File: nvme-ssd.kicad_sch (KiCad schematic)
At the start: 20 parts, among them J3 1-2199230-6

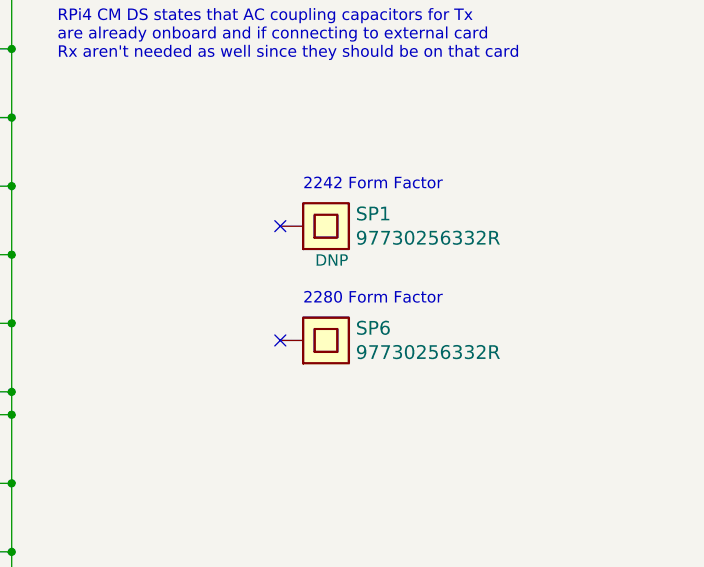
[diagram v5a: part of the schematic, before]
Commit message: Update SP1, SP6 symbol and footprint
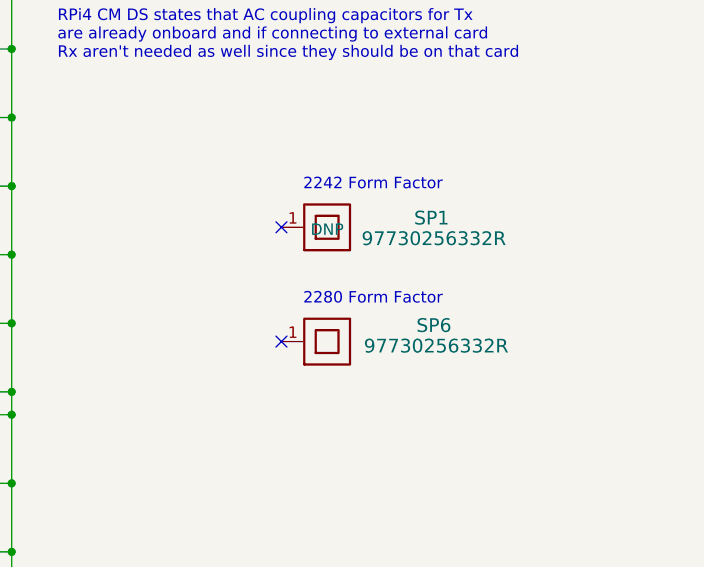
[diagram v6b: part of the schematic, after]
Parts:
- SP1, SP6: footprint scalenode-cm4-baseboard-footprints:97730256332R -> antmicro-footprints:97730256332R; symbol scalenode-cm4-baseboard:97730256332R -> antmicroMechanicalParts:97730256332R; Author (none) -> Antmicro; License (none) -> Apache-2.0; Manufacturer Wurth Elektronik -> Würth Elektronik
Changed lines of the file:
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@@
   (no_connect (at 133.35 85.09))
   (no_connect (at 133.35 52.07))
-  (no_connect (at 211.455 125.095))
+  (no_connect (at 211.582 125.222))
   (no_connect (at 171.45 120.65))
-  (no_connect (at 211.455 112.395))
+  (no_connect (at 211.582 112.522))
   (no_connect (at 171.45 102.87))
   (no_connect (at 171.45 95.25))
@@
     (pin "2")
   )
-  (symbol (lib_id "scalenode-cm4-baseboard:97730256332R") (at 216.535 112.395 0) (unit 1)
+  (symbol (lib_id "antmicroMechanicalParts:97730256332R") (at 211.582 112.522 0) (unit 1)
     (in_bom yes) (on_board yes)
-    (property "Reference" "SP1" (id 0) (at 219.837 111.0488 0)
+    (property "Reference" "SP1" (id 0) (at 226.314 111.506 0)
       (effects (font (size 1.524 1.524)) (justify left))
     )
-    (property "Value" "97730256332R" (id 1) (at 219.837 113.7412 0)
+    (property "Value" "97730256332R" (id 1) (at 220.472 113.792 0)
       (effects (font (size 1.524 1.524)) (justify left))
     )
-    (property "Footprint" "scalenode-cm4-baseboard-footprints:97730256332R" (id 2) (at 220.345 106.045 0)
-      (effects (font (size 1.524 1.524)) hide)
+    (property "Footprint" "antmicro-footprints:97730256332R" (id 2) (at 234.442 120.142 0)
+      (effects (font (size 1.27 1.27) (thickness 0.15)) (justify left bottom) hide)
     )
-    (property "Datasheet" "" (id 3) (at 216.535 112.395 0)
-      (effects (font (size 1.524 1.524)) hide)
+    (property "Datasheet" "" (id 3) (at 234.442 122.682 0)
+      (effects (font (size 1.27 1.27) (thickness 0.15)) (justify left bottom) hide)
     )
-    (property "Manufacturer" "Wurth Elektronik" (id 4) (at 216.535 112.395 0)
-      (effects (font (size 1.27 1.27)) hide)
+    (property "Manufacturer" "Würth Elektronik" (id 4) (at 234.442 125.222 0)
+      (effects (font (size 1.27 1.27) (thickness 0.15)) (justify left bottom) hide)
     )
-    (property "MPN" "97730256332R" (id 5) (at 216.535 112.395 0)
-      (effects (font (size 1.27 1.27)) hide)
+    (property "MPN" "97730256332R" (id 5) (at 234.442 127.762 0)
+      (effects (font (size 1.27 1.27) (thickness 0.15)) (justify left bottom) hide)
+    )
+    (property "DNP" "DNP" (id 6) (at 216.662 112.776 0))
+    (property "Author" "Antmicro" (id 7) (at 234.442 130.302 0)
+      (effects (font (size 1.27 1.27) (thickness 0.15)) (justify left bottom) hide)
+    )
+    (property "License" "Apache-2.0" (id 8) (at 234.442 132.842 0)
+      (effects (font (size 1.27 1.27) (thickness 0.15)) (justify left bottom) hide)
     )
-    (property "DNP" "DNP" (id 6) (at 217.17 116.205 0))
     (pin "1")
   )
-  (symbol (lib_id "scalenode-cm4-baseboard:97730256332R") (at 216.535 125.095 0) (unit 1)
+  (symbol (lib_id "antmicroMechanicalParts:97730256332R") (at 211.582 125.222 0) (unit 1)
     (in_bom yes) (on_board yes)
-    (property "Reference" "SP6" (id 0) (at 219.837 123.7488 0)
+    (property "Reference" "SP6" (id 0) (at 226.568 123.444 0)
       (effects (font (size 1.524 1.524)) (justify left))
     )
-    (property "Value" "97730256332R" (id 1) (at 219.837 126.4412 0)
+    (property "Value" "97730256332R" (id 1) (at 220.726 125.73 0)
       (effects (font (size 1.524 1.524)) (justify left))
     )
-    (property "Footprint" "scalenode-cm4-baseboard-footprints:97730256332R" (id 2) (at 220.345 118.745 0)
-      (effects (font (size 1.524 1.524)) hide)
+    (property "Footprint" "antmicro-footprints:97730256332R" (id 2) (at 234.442 132.842 0)
+      (effects (font (size 1.27 1.27) (thickness 0.15)) (justify left bottom) hide)
     )
-    (property "Datasheet" "" (id 3) (at 216.535 125.095 0)
-      (effects (font (size 1.524 1.524)) hide)
+    (property "Datasheet" "" (id 3) (at 234.442 135.382 0)
+      (effects (font (size 1.27 1.27) (thickness 0.15)) (justify left bottom) hide)
     )
-    (property "Manufacturer" "Wurth Elektronik" (id 4) (at 216.535 125.095 0)
-      (effects (font (size 1.27 1.27)) hide)
+    (property "Manufacturer" "Würth Elektronik" (id 4) (at 234.442 137.922 0)
+      (effects (font (size 1.27 1.27) (thickness 0.15)) (justify left bottom) hide)
     )
-    (property "MPN" "97730256332R" (id 5) (at 216.535 125.095 0)
-      (effects (font (size 1.27 1.27)) hide)
+    (property "MPN" "97730256332R" (id 5) (at 234.442 140.462 0)
+      (effects (font (size 1.27 1.27) (thickness 0.15)) (justify left bottom) hide)
+    )
+    (property "Author" "Antmicro" (id 6) (at 234.442 143.002 0)
+      (effects (font (size 1.27 1.27) (thickness 0.15)) (justify left bottom) hide)
+    )
+    (property "License" "Apache-2.0" (id 7) (at 234.442 145.542 0)
+      (effects (font (size 1.27 1.27) (thickness 0.15)) (justify left bottom) hide)
     )
     (pin "1")

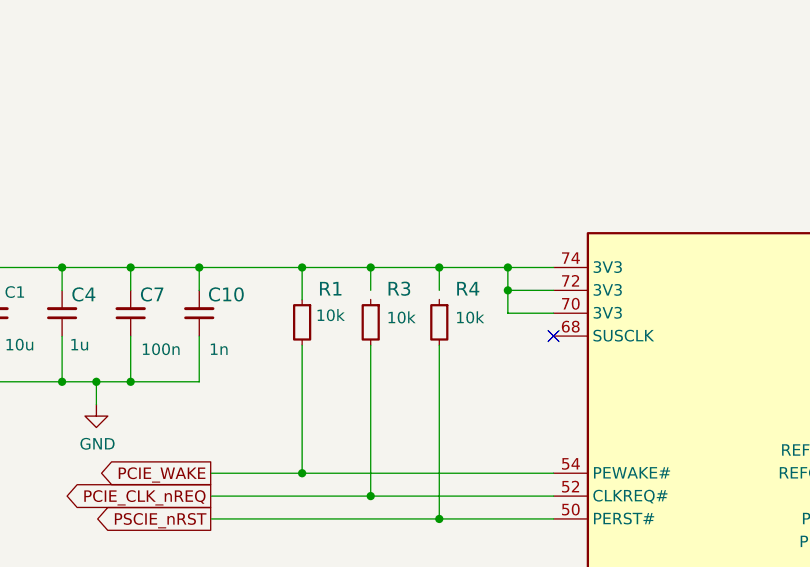
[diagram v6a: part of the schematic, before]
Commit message: Relocate front and back silkscreen labels
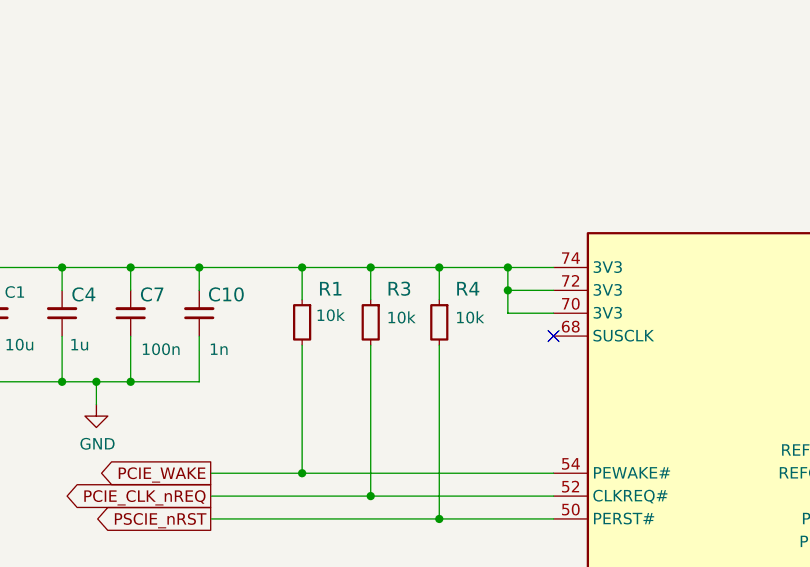
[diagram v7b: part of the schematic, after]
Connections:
- net 3V3_SSD: now also R3.1, R4.1
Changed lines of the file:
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@@
     (stroke (width 0) (type default) (color 0 0 0 0))
   )
-  (wire (pts (xy 120.65 46.99) (xy 120.65 44.45))
+  (wire (pts (xy 120.65 44.45) (xy 120.65 48.006))
     (stroke (width 0) (type default) (color 0 0 0 0))
   )
@@
     (stroke (width 0) (type default) (color 0 0 0 0))
   )
-  (wire (pts (xy 113.03 46.99) (xy 113.03 44.45))
+  (wire (pts (xy 113.03 44.45) (xy 113.03 48.006))
     (stroke (width 0) (type default) (color 0 0 0 0))
   )

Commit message: Remove DRC errors and warnings
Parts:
- SP1, SP6: symbol antmicroMechanicalParts:97730256332R -> antmicroMechanicalParts:Spacer_H0.5mm_97730256332R
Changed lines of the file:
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@@
     (pin "2")
   )
-  (symbol (lib_id "antmicroMechanicalParts:97730256332R") (at 211.582 112.522 0) (unit 1)
+  (symbol (lib_id "antmicroMechanicalParts:Spacer_H0.5mm_97730256332R") (at 211.582 112.522 0) (unit 1)
     (in_bom yes) (on_board yes)
     (property "Reference" "SP1" (id 0) (at 226.314 111.506 0)
@@
       (effects (font (size 1.27 1.27) (thickness 0.15)) (justify left bottom) hide)
     )
-    (property "Datasheet" "" (id 3) (at 234.442 122.682 0)
+    (property "Datasheet" "https://www.we-online.com/components/products/datasheet/97730256332R.pdf" (id 3) (at 234.442 122.682 0)
       (effects (font (size 1.27 1.27) (thickness 0.15)) (justify left bottom) hide)
     )
@@
     (pin "1")
   )
-  (symbol (lib_id "antmicroMechanicalParts:97730256332R") (at 211.582 125.222 0) (unit 1)
+  (symbol (lib_id "antmicroMechanicalParts:Spacer_H0.5mm_97730256332R") (at 211.582 125.222 0) (unit 1)
     (in_bom yes) (on_board yes)
     (property "Reference" "SP6" (id 0) (at 226.568 123.444 0)
@@
       (effects (font (size 1.27 1.27) (thickness 0.15)) (justify left bottom) hide)
     )
-    (property "Datasheet" "" (id 3) (at 234.442 135.382 0)
+    (property "Datasheet" "https://www.we-online.com/components/products/datasheet/97730256332R.pdf" (id 3) (at 234.442 135.382 0)
       (effects (font (size 1.27 1.27) (thickness 0.15)) (justify left bottom) hide)
     )
